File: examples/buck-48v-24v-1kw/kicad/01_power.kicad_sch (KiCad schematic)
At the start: 20 parts, among them J1 VIN+, J2 VIN-, J3 VOUT+, J4 VOUT-, Q1 CSD19536KCS, Q2 CSD19536KCS, Q3 CSD19536KCS, Q4 CSD19536KCS

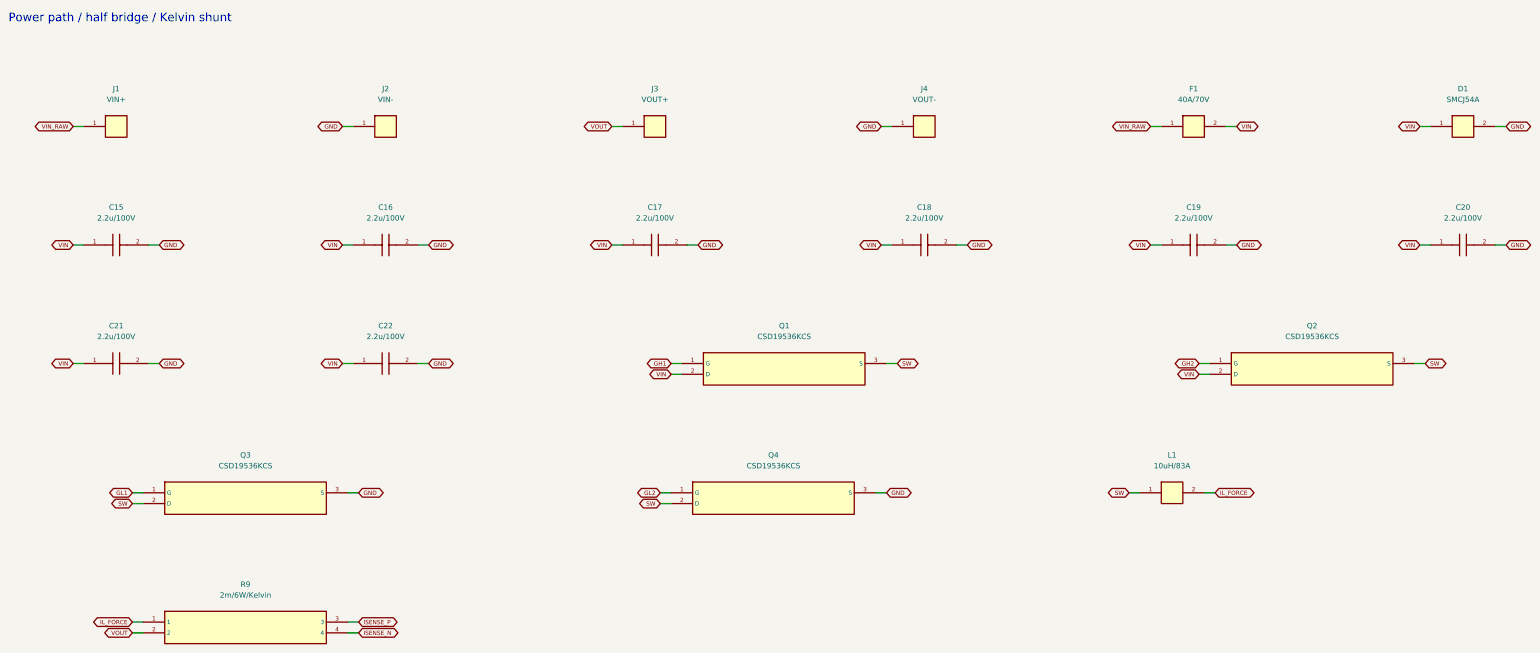
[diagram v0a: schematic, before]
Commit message: feat: complete six-layer power PCB routing and pass native DRC
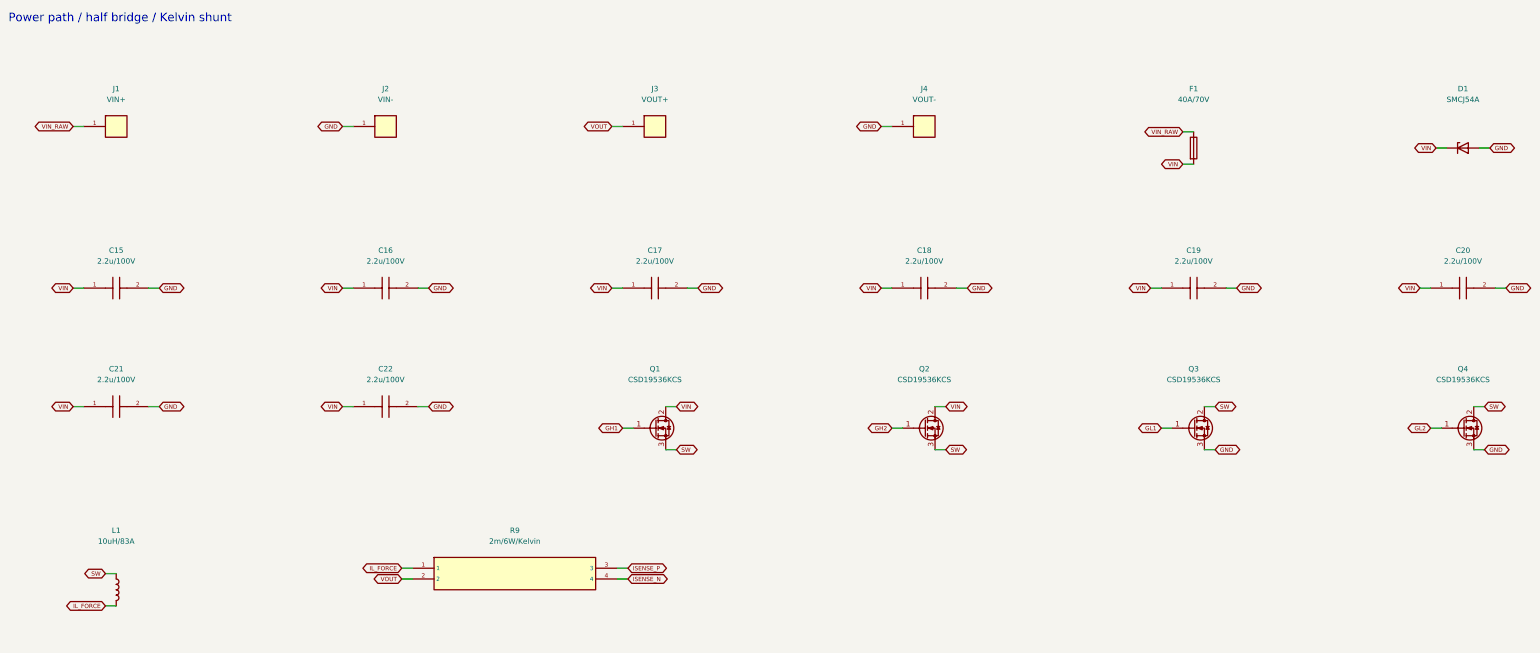
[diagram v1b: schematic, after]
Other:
- moved on the sheet: C15, C16, C17, C18, C19, C20, C21, C22, L1, R9
